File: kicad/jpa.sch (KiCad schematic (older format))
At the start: 4 parts, among them J1 ARM_10PIN, J2 USB-micro-ab, U1 ARM_NOAH_5PIN, U2 PICKIT_HDR

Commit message: schematic done
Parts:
- removed J2: USB-micro-ab, symbol USB-micro-ab
- removed U1: ARM_NOAH_5PIN, symbol ARM_NOAH_5PIN
- removed U2: PICKIT_HDR, symbol PICKIT_HDR
- added J1: ARM_NOAH_6PIN, symbol ARM_NOAH_6PIN
- added J3: ARM_NOAH_5PIN, symbol ARM_NOAH_5PIN
- added J4: PICKIT_HDR, symbol PICKIT_HDR
- renumbered J1 to J2
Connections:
- net labels added: swo/lvp, vcc
- net labels removed: vbus
- wire segments 31 -> 29
- no-connect marks 4 -> 2
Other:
- note added: "Cortex 10-Pin"
- note added: "JST 5-Pin"
- note added: "JST 6-Pin"
- note added: "PIC 6-Pin"
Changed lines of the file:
@@
 LIBS:valves
 LIBS:kicadlib
-LIBS:picUsbProg-cache
 EELAYER 25 0
 EELAYER END
@@
 Comment4 ""
 $EndDescr
-$Comp
-L USB-micro-ab J2
-U 1 1 5638D51B
-P 6350 4750
-F 0 "J2" H 6350 4150 60  0000 C CNN
-F 1 "USB-micro-ab" H 6350 5400 60  0000 C CNN
-F 2 "" H 6350 4750 60  0000 C CNN
-F 3 "" H 6350 4750 60  0000 C CNN
-	1    6350 4750
-	-1   0    0    -1
-$EndComp
-Wire Wire Line
-	5150 4350 6050 4350
-Wire Wire Line
-	5250 4500 6050 4500
-Wire Wire Line
-	5050 4650 6050 4650
-Wire Wire Line
-	5350 4800 6050 4800
-$Comp
-L GND #PWR4
-U 1 1 5638DD9A
-P 5950 5200
-F 0 "#PWR4" H 5950 4950 50  0001 C CNN
-F 1 "GND" H 5950 5050 50  0000 C CNN
-F 2 "" H 5950 5200 60  0000 C CNN
-F 3 "" H 5950 5200 60  0000 C CNN
-	1    5950 5200
-	1    0    0    -1
-$EndComp
-Wire Wire Line
-	6050 4950 5950 4950
-Wire Wire Line
-	5950 4950 5950 5200
-Wire Wire Line
-	6050 5100 5950 5100
-Connection ~ 5950 5100
-$Comp
-L PICKIT_HDR U2
-U 1 1 5638E1BF
-P 4850 4700
-F 0 "U2" H 4450 4150 60  0000 C CNN
-F 1 "PICKIT_HDR" H 4450 5200 60  0000 C CNN
-F 2 "" H 4850 4700 60  0000 C CNN
-F 3 "" H 4850 4700 60  0000 C CNN
-	1    4850 4700
-	1    0    0    -1
-$EndComp
-Text Label 6000 4800 2    60   ~ 0
-icspclk/swdclk
-Text Label 6000 4650 2    60   ~ 0
-mclr/nreset
-Text Label 6000 4500 2    60   ~ 0
-icspdat/swdio
-Text Label 6000 4350 2    60   ~ 0
-vbus
-$Comp
-L GND #PWR3
+Text Label 4950 5500 0    60   ~ 0
+icspclk/swdclk
+Text Label 4950 4900 0    60   ~ 0
+mclr/nreset
+Text Label 4950 5350 0    60   ~ 0
+icspdat/swdio
+Text Label 4950 5050 0    60   ~ 0
+vcc
+$Comp
+L GND #PWR01
 U 1 1 5638E250
-P 4950 5200
-F 0 "#PWR3" H 4950 4950 50  0001 C CNN
-F 1 "GND" H 4950 5050 50  0000 C CNN
-F 2 "" H 4950 5200 60  0000 C CNN
-F 3 "" H 4950 5200 60  0000 C CNN
-	1    4950 5200
-	1    0    0    -1
-$EndComp
-Wire Wire Line
-	4850 4650 4950 4650
-NoConn ~ 4850 5100
-Wire Wire Line
-	5050 4650 5050 4350
-Wire Wire Line
-	5050 4350 4850 4350
-Wire Wire Line
-	4850 4500 5150 4500
-Wire Wire Line
-	5150 4500 5150 4350
-Wire Wire Line
-	4850 4800 5250 4800
-Wire Wire Line
-	5250 4800 5250 4500
-Wire Wire Line
-	5350 4800 5350 4950
-Wire Wire Line
-	5350 4950 4850 4950
-Wire Wire Line
-	4950 4650 4950 5200
-$Comp
-L ARM_10PIN J1
+P 4900 5750
+F 0 "#PWR01" H 4900 5500 50  0001 C CNN
+F 1 "GND" H 4900 5600 50  0000 C CNN
+F 2 "" H 4900 5750 60  0000 C CNN
+F 3 "" H 4900 5750 60  0000 C CNN
+	1    4900 5750
+	1    0    0    -1
+$EndComp
+Wire Wire Line
+	4850 5200 4900 5200
+Wire Wire Line
+	4900 5200 4900 5750
+$Comp
+L ARM_10PIN J2
 U 1 1 5638E4A4
 P 4450 2850
-F 0 "J1" H 4450 1850 60  0000 C CNN
+F 0 "J2" H 4450 1850 60  0000 C CNN
 F 1 "ARM_10PIN" H 4450 3500 60  0000 C CNN
 F 2 "" H 4450 2850 60  0000 C CNN
@@
 $EndComp
 $Comp
-L GND #PWR2
+L GND #PWR02
 U 1 1 5638E672
 P 5000 3800
-F 0 "#PWR2" H 5000 3550 50  0001 C CNN
+F 0 "#PWR02" H 5000 3550 50  0001 C CNN
 F 1 "GND" H 5000 3650 50  0000 C CNN
 F 2 "" H 5000 3800 60  0000 C CNN
@@
 $EndComp
 Wire Wire Line
-	4900 3550 5000 3550
+	5000 3550 4900 3550
 Wire Wire Line
 	5000 2650 5000 3800
@@
 	4900 2650 5000 2650
 Connection ~ 5000 2950
-NoConn ~ 4950 3100
 NoConn ~ 4900 3250
 NoConn ~ 4950 3400
+Text Label 5050 2500 0    60   ~ 0
+icspdat/swdio
+Text Label 5050 2800 0    60   ~ 0
+icspclk/swdclk
+Text Label 5050 3700 0    60   ~ 0
+mclr/nreset
+Wire Wire Line
+	5050 3700 4950 3700
+Wire Wire Line
+	5050 2800 4950 2800
+Wire Wire Line
+	4950 2500 5050 2500
+Wire Wire Line
+	5050 2350 4900 2350
+Text Label 7550 4550 0    60   ~ 0
+icspdat/swdio
+Text Label 7550 4700 0    60   ~ 0
+icspclk/swdclk
+Text Label 7550 4850 0    60   ~ 0
+mclr/nreset
+$Comp
+L GND #PWR03
+U 1 1 5638EF5C
+P 7550 5100
+F 0 "#PWR03" H 7550 4850 50  0001 C CNN
+F 1 "GND" H 7550 4950 50  0000 C CNN
+F 2 "" H 7550 5100 60  0000 C CNN
+F 3 "" H 7550 5100 60  0000 C CNN
+	1    7550 5100
+	1    0    0    -1
+$EndComp
+Wire Wire Line
+	7550 5100 7550 5000
+Wire Wire Line
+	7550 5000 7450 5000
+Wire Wire Line
+	7450 4850 7550 4850
+Wire Wire Line
+	7550 4400 7450 4400
+Wire Wire Line
+	7450 4550 7550 4550
+Wire Wire Line
+	7550 4700 7450 4700
 Text Label 5050 2350 0    60   ~ 0
-vbus
-Text Label 5050 2500 0    60   ~ 0
-icspdat/swdio
-Text Label 5050 2800 0    60   ~ 0
-icspclk/swdclk
-Text Label 5050 3700 0    60   ~ 0
-mclr/nreset
-Wire Wire Line
-	5050 3700 4950 3700
-Wire Wire Line
-	5050 2800 4950 2800
-Wire Wire Line
-	4950 2500 5050 2500
-Wire Wire Line
-	5050 2350 4900 2350
-$Comp
-L ARM_NOAH_5PIN U1
-U 1 1 5638EC7B
-P 5050 1250
-F 0 "U1" H 4650 700 60  0000 C CNN
-F 1 "ARM_NOAH_5PIN" H 4650 1600 60  0000 C CNN
-F 2 "" H 5050 1250 60  0000 C CNN
-F 3 "" H 5050 1250 60  0000 C CNN
-	1    5050 1250
-	1    0    0    -1
-$EndComp
-Text Label 5150 1050 0    60   ~ 0
-vbus
-Text Label 5150 1200 0    60   ~ 0
-icspdat/swdio
-Text Label 5150 1350 0    60   ~ 0
-icspclk/swdclk
-Text Label 5150 1500 0    60   ~ 0
-mclr/nreset
-$Comp
-L GND #PWR1
-U 1 1 5638EF5C
-P 5150 1750
-F 0 "#PWR1" H 5150 1500 50  0001 C CNN
-F 1 "GND" H 5150 1600 50  0000 C CNN
-F 2 "" H 5150 1750 60  0000 C CNN
-F 3 "" H 5150 1750 60  0000 C CNN
-	1    5150 1750
-	1    0    0    -1
-$EndComp
-Wire Wire Line
-	5150 1750 5150 1650
-Wire Wire Line
-	5150 1650 5050 1650
-Wire Wire Line
-	5050 1500 5150 1500
-Wire Wire Line
-	5150 1050 5050 1050
-Wire Wire Line
-	5050 1200 5150 1200
-Wire Wire Line
-	5150 1350 5050 1350
+vcc
+Text Label 7550 4400 0    60   ~ 0
+vcc
+Wire Wire Line
+	4950 5500 4850 5500
+Wire Wire Line
+	4950 5350 4850 5350
+Wire Wire Line
+	4950 5050 4850 5050
+Wire Wire Line
+	4950 4900 4850 4900
+Text Label 5050 3100 0    60   ~ 0
+swo/lvp
+Wire Wire Line
+	5050 3100 4950 3100
+$Comp
+L ARM_NOAH_5PIN J3
+U 1 1 563A3135
+P 7450 4600
+F 0 "J3" H 7050 4050 60  0000 C CNN
+F 1 "ARM_NOAH_5PIN" H 7050 4950 60  0000 C CNN
+F 2 "" H 7450 4600 60  0000 C CNN
+F 3 "" H 7450 4600 60  0000 C CNN
+	1    7450 4600
+	1    0    0    -1
+$EndComp
+$Comp
+L PICKIT_HDR J4
+U 1 1 563A32E2
+P 4850 5250
+F 0 "J4" H 4450 4700 60  0000 C CNN
+F 1 "PICKIT_HDR" H 4450 5750 60  0000 C CNN
+F 2 "" H 4850 5250 60  0000 C CNN
+F 3 "" H 4850 5250 60  0000 C CNN
+	1    4850 5250
+	1    0    0    -1
+$EndComp
+$Comp
+L ARM_NOAH_6PIN J1
+U 1 1 563A335E
+P 7400 2700
+F 0 "J1" H 7050 2000 60  0000 C CNN
+F 1 "ARM_NOAH_6PIN" H 7050 3050 60  0000 C CNN
+F 2 "" H 7400 2700 60  0000 C CNN
+F 3 "" H 7400 2700 60  0000 C CNN
+	1    7400 2700
+	1    0    0    -1
+$EndComp
+Text Notes 4200 2000 0    60   ~ 0
+Cortex 10-Pin
+Text Notes 4250 4550 0    60   ~ 0
+PIC 6-Pin
+Text Label 4950 5650 0    60   ~ 0
+swo/lvp
+Wire Wire Line
+	4850 5650 4950 5650
+Text Label 7500 3250 0    60   ~ 0
+swo/lvp
+Text Label 7500 2650 0    60   ~ 0
+icspdat/swdio
+Text Label 7500 2800 0    60   ~ 0
+icspclk/swdclk
+Text Label 7500 2950 0    60   ~ 0
+mclr/nreset
+Text Label 7500 2500 0    60   ~ 0
+vcc
+$Comp
+L GND #PWR04
+U 1 1 563A34DE
+P 7450 3350
+F 0 "#PWR04" H 7450 3100 50  0001 C CNN
+F 1 "GND" H 7450 3200 50  0000 C CNN
+F 2 "" H 7450 3350 60  0000 C CNN
+F 3 "" H 7450 3350 60  0000 C CNN
+	1    7450 3350
+	1    0    0    -1
+$EndComp
+Wire Wire Line
+	7450 3350 7450 3100
+Wire Wire Line
+	7450 3100 7400 3100
+Wire Wire Line
+	7400 3250 7500 3250
+Wire Wire Line
+	7500 2950 7400 2950
+Wire Wire Line
+	7400 2800 7500 2800
+Wire Wire Line
+	7500 2650 7400 2650
+Wire Wire Line
+	7400 2500 7500 2500
+Text Notes 6900 2150 0    60   ~ 0
+JST 6-Pin
+Text Notes 6900 4050 0    60   ~ 0
+JST 5-Pin
+Wire Notes Line
+	3900 1800 3900 4100
+Wire Notes Line
+	3900 4100 5900 4100
+Wire Notes Line
+	5900 4100 5900 1800
+Wire Notes Line
+	5900 1800 3900 1800
+Wire Notes Line
+	4000 4350 5750 4350
+Wire Notes Line
+	5750 4350 5750 6050
+Wire Notes Line
+	5750 6050 4000 6050
+Wire Notes Line
+	4000 6050 4000 4350
+Wire Notes Line
+	6550 3850 8350 3850
+Wire Notes Line
+	8350 3850 8350 5400
+Wire Notes Line
+	8350 5400 6550 5400
+Wire Notes Line
+	6550 5400 6550 3850
+Wire Notes Line
+	6550 1900 6550 3650
+Wire Notes Line
+	6550 3650 8350 3650
+Wire Notes Line
+	8350 3650 8350 1900
+Wire Notes Line
+	8350 1900 6550 1900
 $EndSCHEMATC

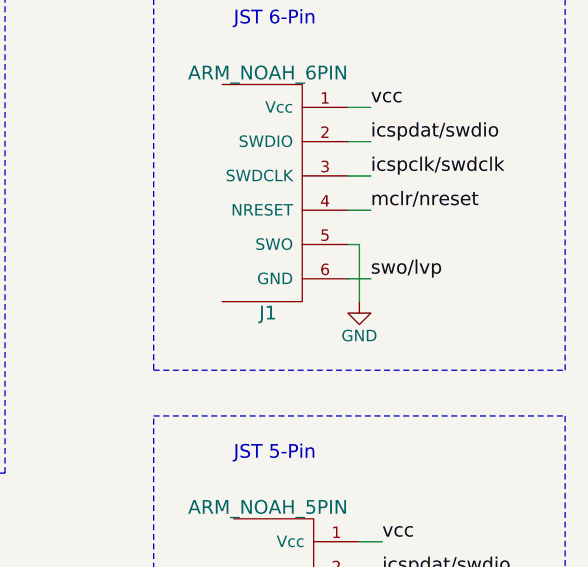
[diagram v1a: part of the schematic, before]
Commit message: update arm 6-pin header
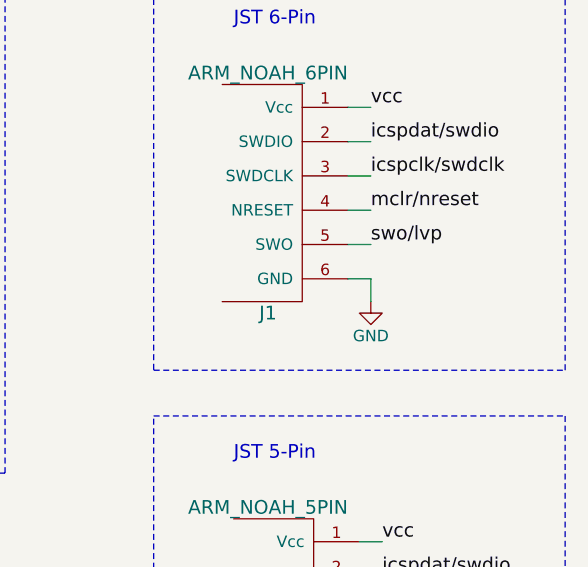
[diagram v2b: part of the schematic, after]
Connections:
- net GND: now also J1.6 (GND); no longer J1.5 (SWO)
- net swo/lvp: now also J1.5 (SWO); no longer J1.6 (GND)
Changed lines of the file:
@@
 LIBS:valves
 LIBS:kicadlib
+LIBS:jpa-cache
 EELAYER 25 0
 EELAYER END
@@
 vcc
 $Comp
-L GND #PWR01
+L GND #PWR4
 U 1 1 5638E250
 P 4900 5750
-F 0 "#PWR01" H 4900 5500 50  0001 C CNN
+F 0 "#PWR4" H 4900 5500 50  0001 C CNN
 F 1 "GND" H 4900 5600 50  0000 C CNN
 F 2 "" H 4900 5750 60  0000 C CNN
@@
 $EndComp
 $Comp
-L GND #PWR02
+L GND #PWR2
 U 1 1 5638E672
 P 5000 3800
-F 0 "#PWR02" H 5000 3550 50  0001 C CNN
+F 0 "#PWR2" H 5000 3550 50  0001 C CNN
 F 1 "GND" H 5000 3650 50  0000 C CNN
 F 2 "" H 5000 3800 60  0000 C CNN
@@
 mclr/nreset
 $Comp
-L GND #PWR03
+L GND #PWR3
 U 1 1 5638EF5C
 P 7550 5100
-F 0 "#PWR03" H 7550 4850 50  0001 C CNN
+F 0 "#PWR3" H 7550 4850 50  0001 C CNN
 F 1 "GND" H 7550 4950 50  0000 C CNN
 F 2 "" H 7550 5100 60  0000 C CNN
@@
 	1    0    0    -1
 $EndComp
+Text Notes 4200 2000 0    60   ~ 0
+Cortex 10-Pin
+Text Notes 4250 4550 0    60   ~ 0
+PIC 6-Pin
+Text Label 4950 5650 0    60   ~ 0
+swo/lvp
+Wire Wire Line
+	4850 5650 4950 5650
+Text Label 7500 3100 0    60   ~ 0
+swo/lvp
+Text Label 7500 2650 0    60   ~ 0
+icspdat/swdio
+Text Label 7500 2800 0    60   ~ 0
+icspclk/swdclk
+Text Label 7500 2950 0    60   ~ 0
+mclr/nreset
+Text Label 7500 2500 0    60   ~ 0
+vcc
+$Comp
+L GND #PWR1
+U 1 1 563A34DE
+P 7500 3350
+F 0 "#PWR1" H 7500 3100 50  0001 C CNN
+F 1 "GND" H 7500 3200 50  0000 C CNN
+F 2 "" H 7500 3350 60  0000 C CNN
+F 3 "" H 7500 3350 60  0000 C CNN
+	1    7500 3350
+	1    0    0    -1
+$EndComp
+Wire Wire Line
+	7400 3100 7500 3100
+Wire Wire Line
+	7500 2950 7400 2950
+Wire Wire Line
+	7400 2800 7500 2800
+Wire Wire Line
+	7500 2650 7400 2650
+Wire Wire Line
+	7400 2500 7500 2500
+Text Notes 6900 2150 0    60   ~ 0
+JST 6-Pin
+Text Notes 6900 4050 0    60   ~ 0
+JST 5-Pin
+Wire Notes Line
+	3900 1800 3900 4100
+Wire Notes Line
+	3900 4100 5900 4100
+Wire Notes Line
+	5900 4100 5900 1800
+Wire Notes Line
+	5900 1800 3900 1800
+Wire Notes Line
+	4000 4350 5750 4350
+Wire Notes Line
+	5750 4350 5750 6050
+Wire Notes Line
+	5750 6050 4000 6050
+Wire Notes Line
+	4000 6050 4000 4350
+Wire Notes Line
+	6550 3850 8350 3850
+Wire Notes Line
+	8350 3850 8350 5400
+Wire Notes Line
+	8350 5400 6550 5400
+Wire Notes Line
+	6550 5400 6550 3850
+Wire Notes Line
+	6550 1900 6550 3650
+Wire Notes Line
+	6550 3650 8350 3650
+Wire Notes Line
+	8350 3650 8350 1900
+Wire Notes Line
+	8350 1900 6550 1900
 $Comp
 L ARM_NOAH_6PIN J1
-U 1 1 563A335E
+U 1 1 564209BA
 P 7400 2700
 F 0 "J1" H 7050 2000 60  0000 C CNN
@@
 	1    0    0    -1
 $EndComp
-Text Notes 4200 2000 0    60   ~ 0
-Cortex 10-Pin
-Text Notes 4250 4550 0    60   ~ 0
-PIC 6-Pin
-Text Label 4950 5650 0    60   ~ 0
-swo/lvp
-Wire Wire Line
-	4850 5650 4950 5650
-Text Label 7500 3250 0    60   ~ 0
-swo/lvp
-Text Label 7500 2650 0    60   ~ 0
-icspdat/swdio
-Text Label 7500 2800 0    60   ~ 0
-icspclk/swdclk
-Text Label 7500 2950 0    60   ~ 0
-mclr/nreset
-Text Label 7500 2500 0    60   ~ 0
-vcc
-$Comp
-L GND #PWR04
-U 1 1 563A34DE
-P 7450 3350
-F 0 "#PWR04" H 7450 3100 50  0001 C CNN
-F 1 "GND" H 7450 3200 50  0000 C CNN
-F 2 "" H 7450 3350 60  0000 C CNN
-F 3 "" H 7450 3350 60  0000 C CNN
-	1    7450 3350
-	1    0    0    -1
-$EndComp
-Wire Wire Line
-	7450 3350 7450 3100
-Wire Wire Line
-	7450 3100 7400 3100
-Wire Wire Line
-	7400 3250 7500 3250
-Wire Wire Line
-	7500 2950 7400 2950
-Wire Wire Line
-	7400 2800 7500 2800
-Wire Wire Line
-	7500 2650 7400 2650
-Wire Wire Line
-	7400 2500 7500 2500
-Text Notes 6900 2150 0    60   ~ 0
-JST 6-Pin
-Text Notes 6900 4050 0    60   ~ 0
-JST 5-Pin
-Wire Notes Line
-	3900 1800 3900 4100
-Wire Notes Line
-	3900 4100 5900 4100
-Wire Notes Line
-	5900 4100 5900 1800
-Wire Notes Line
-	5900 1800 3900 1800
-Wire Notes Line
-	4000 4350 5750 4350
-Wire Notes Line
-	5750 4350 5750 6050
-Wire Notes Line
-	5750 6050 4000 6050
-Wire Notes Line
-	4000 6050 4000 4350
-Wire Notes Line
-	6550 3850 8350 3850
-Wire Notes Line
-	8350 3850 8350 5400
-Wire Notes Line
-	8350 5400 6550 5400
-Wire Notes Line
-	6550 5400 6550 3850
-Wire Notes Line
-	6550 1900 6550 3650
-Wire Notes Line
-	6550 3650 8350 3650
-Wire Notes Line
-	8350 3650 8350 1900
-Wire Notes Line
-	8350 1900 6550 1900
+Wire Wire Line
+	7500 3350 7500 3250
+Wire Wire Line
+	7500 3250 7400 3250
 $EndSCHEMATC

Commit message: place components, still need a footprint for pic connector
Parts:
- J1: footprint (none) -> kicadlib:SMD_JST_6_PIN_VERT
- J2: footprint (none) -> kicadlib:ARM_10_PIN
- J3: footprint (none) -> kicadlib:SMD_JST_5_PIN_VERT
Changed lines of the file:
@@
 vcc
 $Comp
-L GND #PWR4
+L GND #PWR01
 U 1 1 5638E250
 P 4900 5750
-F 0 "#PWR4" H 4900 5500 50  0001 C CNN
+F 0 "#PWR01" H 4900 5500 50  0001 C CNN
 F 1 "GND" H 4900 5600 50  0000 C CNN
 F 2 "" H 4900 5750 60  0000 C CNN
@@
 F 0 "J2" H 4450 1850 60  0000 C CNN
 F 1 "ARM_10PIN" H 4450 3500 60  0000 C CNN
-F 2 "" H 4450 2850 60  0000 C CNN
+F 2 "kicadlib:ARM_10_PIN" H 4450 2850 60  0001 C CNN
 F 3 "" H 4450 2850 60  0000 C CNN
 	1    4450 2850
@@
 $EndComp
 $Comp
-L GND #PWR2
+L GND #PWR02
 U 1 1 5638E672
 P 5000 3800
-F 0 "#PWR2" H 5000 3550 50  0001 C CNN
+F 0 "#PWR02" H 5000 3550 50  0001 C CNN
 F 1 "GND" H 5000 3650 50  0000 C CNN
 F 2 "" H 5000 3800 60  0000 C CNN
@@
 mclr/nreset
 $Comp
-L GND #PWR3
+L GND #PWR03
 U 1 1 5638EF5C
 P 7550 5100
-F 0 "#PWR3" H 7550 4850 50  0001 C CNN
+F 0 "#PWR03" H 7550 4850 50  0001 C CNN
 F 1 "GND" H 7550 4950 50  0000 C CNN
 F 2 "" H 7550 5100 60  0000 C CNN
@@
 F 0 "J3" H 7050 4050 60  0000 C CNN
 F 1 "ARM_NOAH_5PIN" H 7050 4950 60  0000 C CNN
-F 2 "" H 7450 4600 60  0000 C CNN
+F 2 "kicadlib:SMD_JST_5_PIN_VERT" H 7450 4600 60  0001 C CNN
 F 3 "" H 7450 4600 60  0000 C CNN
 	1    7450 4600
@@
 F 0 "J4" H 4450 4700 60  0000 C CNN
 F 1 "PICKIT_HDR" H 4450 5750 60  0000 C CNN
-F 2 "" H 4850 5250 60  0000 C CNN
+F 2 "" H 4850 5250 60  0001 C CNN
 F 3 "" H 4850 5250 60  0000 C CNN
 	1    4850 5250
@@
 vcc
 $Comp
-L GND #PWR1
+L GND #PWR04
 U 1 1 563A34DE
 P 7500 3350
-F 0 "#PWR1" H 7500 3100 50  0001 C CNN
+F 0 "#PWR04" H 7500 3100 50  0001 C CNN
 F 1 "GND" H 7500 3200 50  0000 C CNN
 F 2 "" H 7500 3350 60  0000 C CNN
@@
 F 0 "J1" H 7050 2000 60  0000 C CNN
 F 1 "ARM_NOAH_6PIN" H 7050 3050 60  0000 C CNN
-F 2 "" H 7400 2700 60  0000 C CNN
+F 2 "kicadlib:SMD_JST_6_PIN_VERT" H 7400 2700 60  0001 C CNN
 F 3 "" H 7400 2700 60  0000 C CNN
 	1    7400 2700

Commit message: layout, gerbers, models done
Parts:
- J4: footprint (none) -> kicadlib:TH_6X1_HDR
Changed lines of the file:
@@
 LIBS:valves
 LIBS:kicadlib
-LIBS:jpa-cache
 EELAYER 25 0
 EELAYER END
@@
 F 0 "J4" H 4450 4700 60  0000 C CNN
 F 1 "PICKIT_HDR" H 4450 5750 60  0000 C CNN
-F 2 "" H 4850 5250 60  0001 C CNN
+F 2 "kicadlib:TH_6X1_HDR" H 4850 5250 60  0001 C CNN
 F 3 "" H 4850 5250 60  0000 C CNN
 	1    4850 5250
